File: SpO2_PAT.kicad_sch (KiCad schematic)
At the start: 0 parts

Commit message: top-level structure and ESP32-C6 pin assignments nearly sorted
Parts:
- added NT4: NetTie_2, NetTie:NetTie-2_SMD_Pad0.5mm, symbol Device:NetTie_2
- added U10: ADS1115IDGS, Package_SO:TSSOP-10_3x3mm_P0.5mm, symbol Analog_ADC:ADS1115IDGS
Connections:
- new net: NT4.1, U10.1 (ADDR)
- new net AIN3: U10.7 (AIN3)
- new net GND: NT4.2, U10.3 (GND)
- new net SCL: U10.10 (SCL)
- new net SDA: U10.9 (SDA)
- new net VDD: U10.8 (VDD)
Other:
- note added: "I2C address = 0x48"
- company: (none) -> Sunrise designs
- title: (none) -> Open polysomnography board

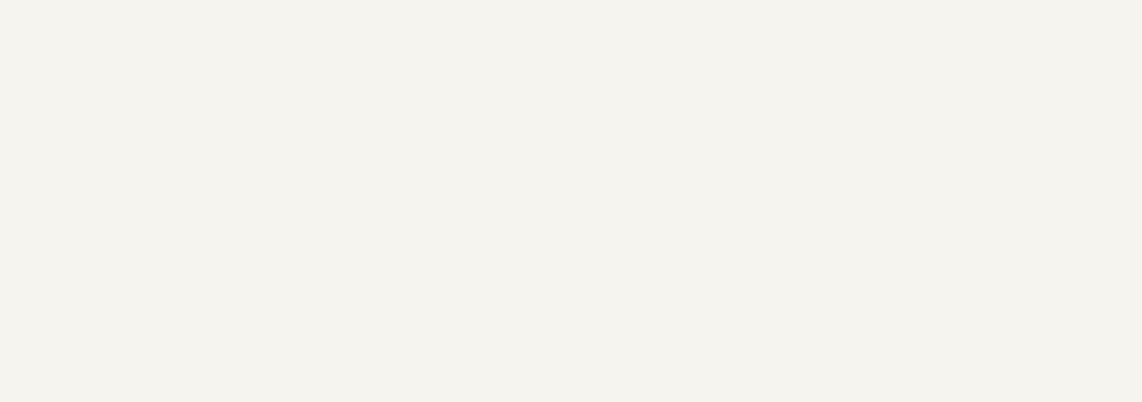
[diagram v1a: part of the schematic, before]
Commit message: text comments sections added
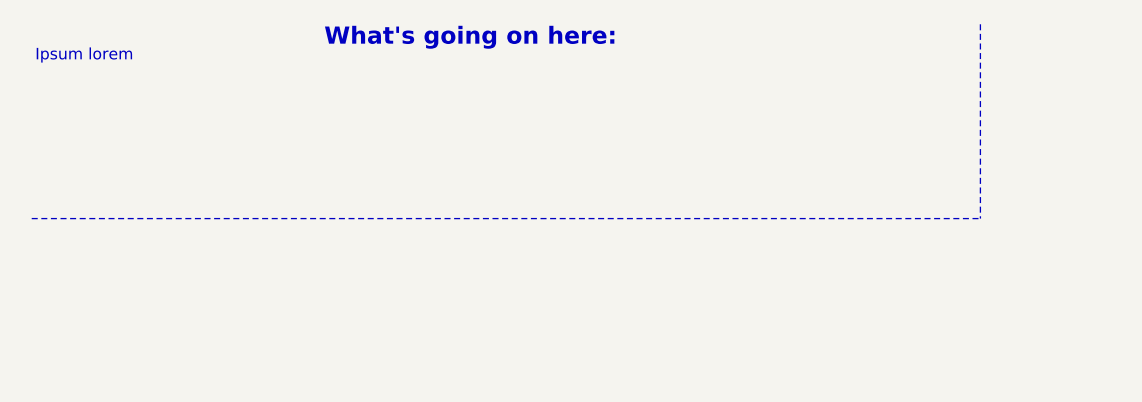
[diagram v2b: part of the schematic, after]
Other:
- note added: "Ipsum lorem"
- note added: "What's going on here:"
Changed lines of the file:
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@@
 		(company "Sunrise designs")
+	)
+	(text "What's going on here:\n"
+		(exclude_from_sim no)
+		(at 61.468 14.224 0)
+		(effects
+			(font
+				(size 1.905 1.905)
+				(thickness 0.381)
+				(bold yes)
+				(color 132 0 0 1)
+			)
+		)
 	)
 	(text "I2C address = 0x48"
@@
 		)
 	)
+	(text "Ipsum lorem\n"
+		(exclude_from_sim no)
+		(at 18.542 16.256 0)
+		(effects
+			(font
+				(size 1.27 1.27)
+				(color 132 0 0 1)
+			)
+		)
+	)
 	(junction
 		(at 133.35 97.79)
 		(diameter 0)
 		(color 0 0 0 0)
+	)
+	(polyline
+		(pts
+			(xy 12.7 34.29) (xy 118.11 34.29)
+		)
+		(stroke
+			(width 0)
+			(type dash)
+			(color 132 0 0 1)
+		)
 	)
 	(wire
@@
 		)
 	)
+	(polyline
+		(pts
+			(xy 118.11 12.7) (xy 118.11 34.29)
+		)
+		(stroke
+			(width 0)
+			(type dash)
+			(color 132 0 0 1)
+		)
+	)

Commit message: some work on sch and docs added
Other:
- note added: "BH1750 (Can probably just use a photodiode + an ADC channel)"
- note added: "Texas Instruments TMP102AIDRLR (or can use an NTC)"
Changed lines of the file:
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@@
+		)
+	)
+	(text "Texas Instruments\nTMP102AIDRLR (or can use an NTC)"
+		(exclude_from_sim no)
+		(at 97.282 121.158 0)
+		(effects
+			(font
+				(size 1.27 1.27)
+			)
+		)
+	)
+	(text "BH1750\n(Can probably just use a photodiode + an ADC channel)"
+		(exclude_from_sim no)
+		(at 96.774 105.664 0)
+		(effects
+			(font
+				(size 1.27 1.27)
+			)
 		)
 	)
